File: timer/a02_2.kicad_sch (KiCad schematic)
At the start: 20 parts, among them U2042 74HC04, U2043 74HC4002, U2044 74HC02, U2102 74HC27, U2104 74HC02, U2107 74HC27, U2111 74HC27, U2112 74HC02, U2113 74HC02, U2114 74HC02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

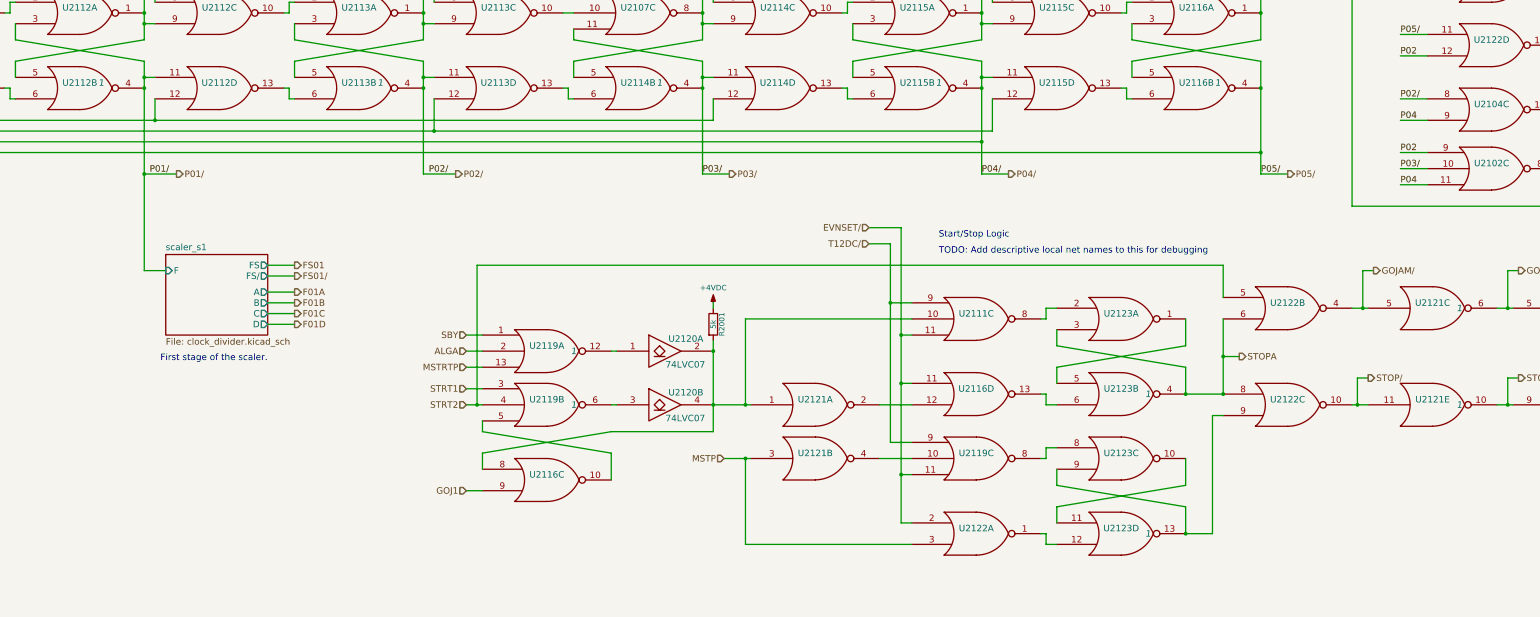
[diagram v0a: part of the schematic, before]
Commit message: Added Init values
Added individual Init Values for Components. TImer Module Updated with init values
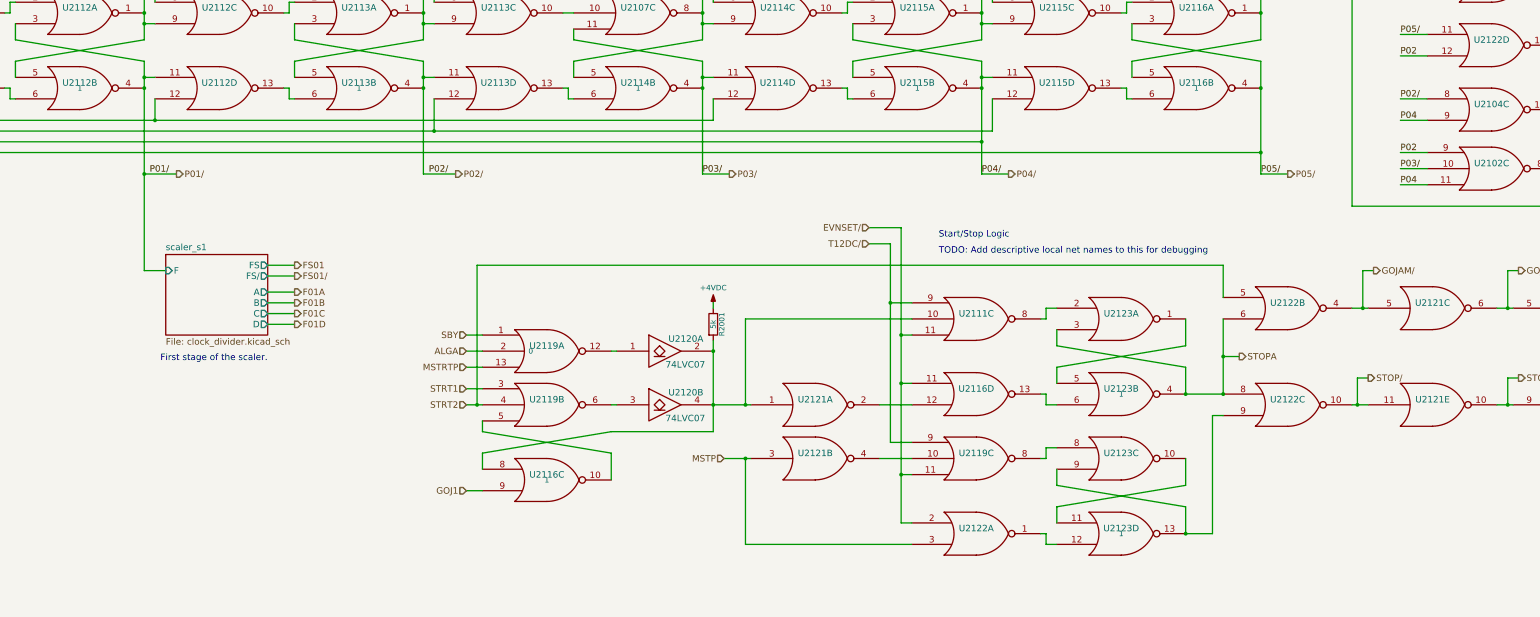
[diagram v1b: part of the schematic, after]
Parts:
- U2042, U2121, U2145: Init_A (none) -> 0; Init_B (none) -> 0; Init_C (none) -> 0; Init_D (none) -> 0; Init_E (none) -> 0; Init_F (none) -> 0
- U2044, U2104, U2107, U2111, U2119, U2122: Init_A (none) -> 0; Init_B (none) -> 0; Init_C (none) -> 0; Init_D (none) -> 0
- U2102, U2112, U2113, U2114, U2115: Init_A (none) -> 0; Init_B (none) -> 1; Init_C (none) -> 0; Init_D (none) -> 0
- U2112, U2113, U2114, U2115: Init_A (none) -> 0; Init_B (none) -> 1; Init_C (none) -> 0; Init_D (none) -> 0; Initial 1 -> (none)
- U2116: Init_A (none) -> 0; Init_B (none) -> 1; Init_C (none) -> 1; Init_D (none) -> 0
- U2116: Init_A (none) -> 0; Init_B (none) -> 1; Init_C (none) -> 1; Init_D (none) -> 0; Initial 1 -> (none)
- U2119: Init_A (none) -> 0; Init_B (none) -> 0; Init_C (none) -> 0; Init_D (none) -> 0; Initial 1 -> (none)
- U2121: Init_A (none) -> 0; Init_B (none) -> 0; Init_C (none) -> 0; Init_D (none) -> 0; Init_E (none) -> 0; Init_F (none) -> 0; Initial 1 -> (none)
- U2123: Init_A (none) -> 0; Init_B (none) -> 1; Init_C (none) -> 0; Init_D (none) -> 1
- U2123: Init_A (none) -> 0; Init_B (none) -> 1; Init_C (none) -> 0; Init_D (none) -> 1; Initial 1 -> (none)
